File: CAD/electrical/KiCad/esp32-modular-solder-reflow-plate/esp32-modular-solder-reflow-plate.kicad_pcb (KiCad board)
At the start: 2 copper layers, 81.3 x 50.8 mm, 86 parts, among them J1 Thermo Coupler JST, J2 HEATER P, J3 HEATER N, J4 Micro_SD, J5 USB-C, J6 I2C, J7 PWR_IN, J8 Serial, Q1 Heater N-FET, Q2 Q_PMOS_DGS, SW1 µC_BTN01, SW2 µC_BTN02, SW3 µC_BTN03, SW4 µC_BTN04, SW5 µC_EN, SW6 µC_IO0, U1 MAX31855KASA, U2 ESP32-S3-WROOM-2, U3 AMS1117-3.3, U4 AMS1117-5.0, Y1 32k Hz

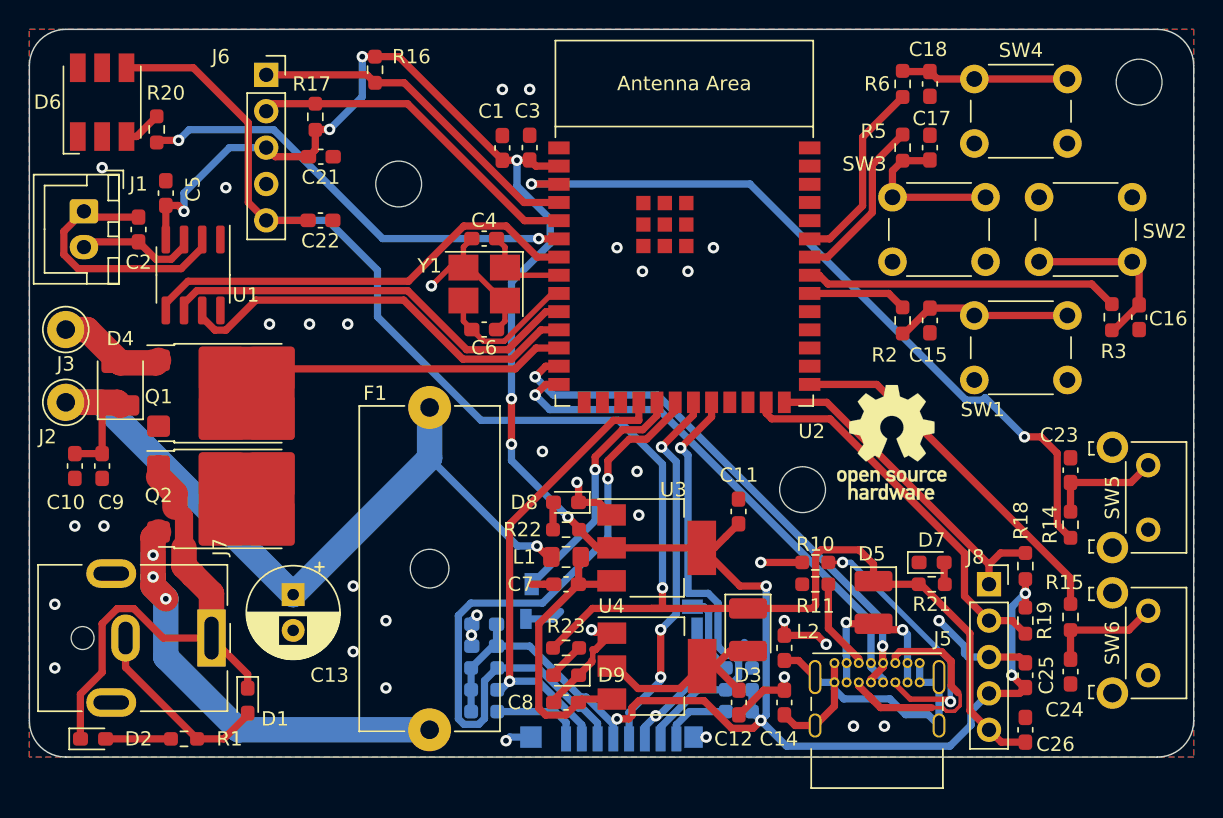
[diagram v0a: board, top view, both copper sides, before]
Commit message: - CAD: pcb routing improvements
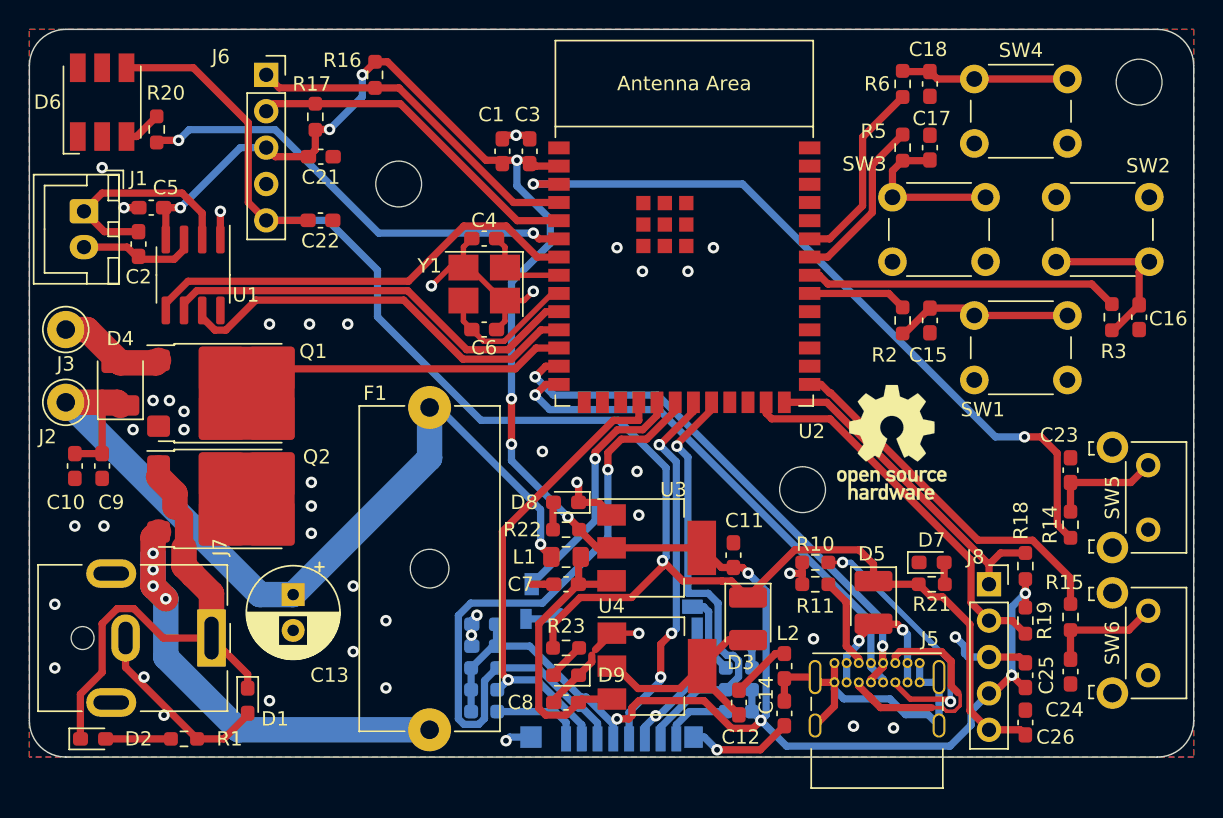
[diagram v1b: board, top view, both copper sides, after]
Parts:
- moved C11 3.07 mm to (172.3, 93.2)
- moved C5 1.44 mm to (131.7, 69.0), turned to 180 degrees
- moved L2 1.27 mm to (175.9, 101.0)
- moved SW2 1.19 mm to (201.4, 72.7)
- moved C2 1.02 mm to (130.8, 71.5)
- moved C14 0.76 mm to (175.9, 104.3), turned to 90 degrees
- moved D3 0.76 mm to (173.4, 97.7)
- moved C26 0.51 mm to (192.7, 104.9)
- moved R16 0.36 mm to (147.3, 59.7)
- moved C3 0.25 mm to (158.1, 65.0)
- moved C1 0.23 mm to (156.2, 65.0)
- turned C12 to 90 degrees
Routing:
- net 3V3_µC: track 162.8 -> 156.7 mm
- net PWR_IN_N: track 80.0 -> 85.0 mm, vias 37 -> 47
- net THCPL_n: track 18.8 -> 15.6 mm
- net HEATER_P: track 59.2 -> 62.1 mm
- net Net-(D3-A): track 13.6 -> 16.0 mm
- net +5V: track 115.1 -> 112.7 mm
- net Net-(D5-A): track 12.2 -> 10.9 mm
- net Net-(J5-SHIELD): track 26.6 -> 25.4 mm
- net Net-(Q2-S): track 33.2 -> 33.3 mm, vias 3 -> 4

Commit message: - CAD: library clean up, routing improvements, new heat bed terminal
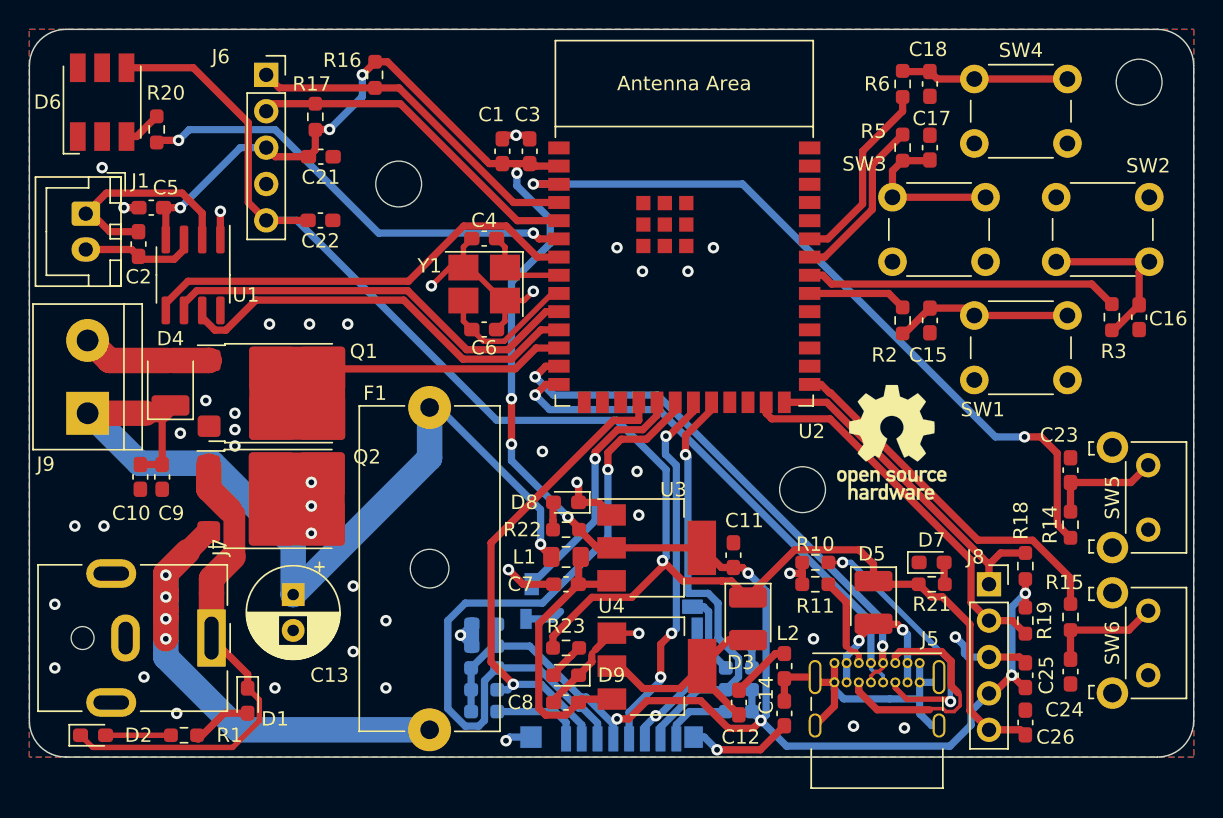
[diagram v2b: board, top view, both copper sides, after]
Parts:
- removed J2: HEATER P, Connector_Pin:Pin_D1.3mm_L11.0mm
- removed J3: HEATER N, Connector_Pin:Pin_D1.3mm_L11.0mm
- added J9: Heater, TerminalBlock:TerminalBlock_bornier-2_P5.08mm, F.Cu at (127.3, 83.3)
- Mount 1: renamed from REF**
- Mount 2: renamed from REF**
- Mount 3: renamed from REF**
- moved C10 4.64 mm to (130.9, 87.8)
- moved C9 4.26 mm to (132.5, 87.8)
- moved Q1 3.53 mm to (140.7, 81.9)
- moved D4 3.50 mm to (133.0, 81.3)
- moved Q2 3.50 mm to (140.7, 89.3)
- moved D2 0.25 mm to (127.6, 105.8)
- moved R1 0.25 mm to (134.0, 105.8)
- moved J1 0.21 mm to (127.1, 69.4)
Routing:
- net PWR_IN_N: track 85.0 -> 79.7 mm
- net HEATER_CTRL: track 20.7 -> 17.1 mm
- net HEATER_P: track 62.1 -> 64.6 mm
- net Net-(Q2-S): track 33.3 -> 35.0 mm
- net +5V: track 112.7 -> 111.0 mm
- net Net-(J5-SHIELD): track 25.4 -> 23.7 mm
- net PWR_IN_P: track 35.7 -> 34.2 mm
- net HEATER_N: track 7.52 -> 8.61 mm
- net SD_CMD: track 48.1 -> 49.1 mm
- net SD_CD: track 33.0 -> 33.8 mm
- net Net-(D9-A): track 2.65 -> 3.40 mm
- net SD_DAT0: track 30.8 -> 30.0 mm
- net USBC_SBU12: track 17.4 -> 16.7 mm
- net THCPL_p: track 8.91 -> 8.27 mm
- net Net-(D8-A): track 1.92 -> 2.55 mm
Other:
- board text added: "Modular Solder Reflow Plate Main Control Board Rev. 0.0.1"

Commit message: - cad: added USB d+ and d- pull up and pull down options; optimized overall component layout; improved silkscreens
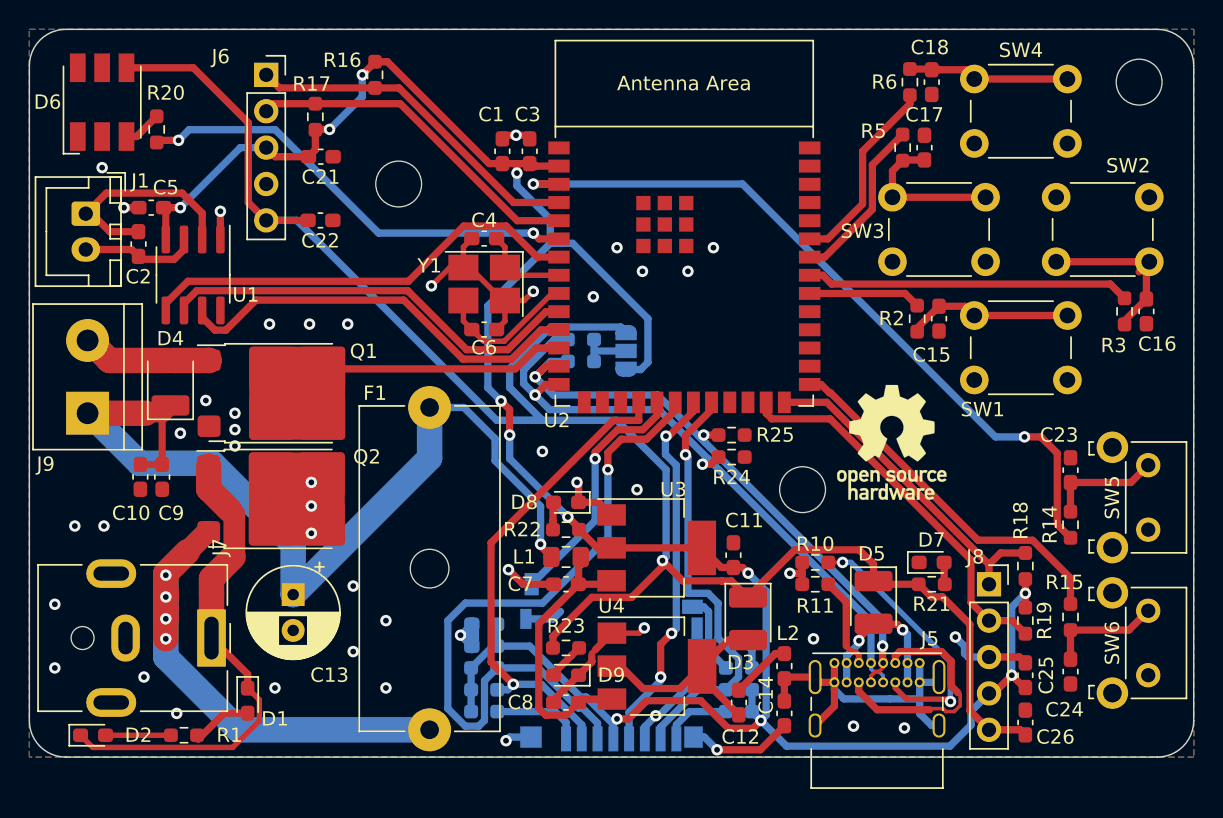
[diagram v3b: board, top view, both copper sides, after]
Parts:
- added JP1: USB_PU, Jumper:SolderJumper-3_P1.3mm_Open_RoundedPad1.0x1.5mm, B.Cu at (164.8, 79.0)
- added R24: 5k1, Resistor_SMD:R_0603_1608Metric_Pad0.98x0.95mm_HandSolder, F.Cu at (172.2, 86.4)
- added R25: 5k1, Resistor_SMD:R_0603_1608Metric_Pad0.98x0.95mm_HandSolder, F.Cu at (172.2, 84.8)
- added R26: 5k1, Resistor_SMD:R_0603_1608Metric_Pad0.98x0.95mm_HandSolder, B.Cu at (161.7, 78.2)
- added R27: 5k1, Resistor_SMD:R_0603_1608Metric_Pad0.98x0.95mm_HandSolder, B.Cu at (161.7, 79.7)
- J1: value Thermo Coupler JST -> Thermo Coupler
- moved R2 1.02 mm to (185.2, 76.7)
- moved R3 0.98 mm to (199.6, 76.2)
- moved C16 0.65 mm to (201.2, 76.2)
- moved C15 0.65 mm to (186.7, 76.7)
- moved R6 0.52 mm to (184.7, 60.2)
- moved C17 0.38 mm to (185.7, 64.8)
- moved C18 0.18 mm to (186.2, 60.2)
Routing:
- net +5V: track 111.0 -> 127.1 mm
- net 3V3_µC: track 156.9 -> 172.1 mm
- net USB_Dp: track 36.8 -> 44.7 mm, vias 1 -> 2
- net USB_Dn: track 38.1 -> 41.9 mm, vias 2 -> 3
- net Net-(JP1-C): track 0.00 -> 3.73 mm
- net HEATER_P: track 64.6 -> 66.3 mm
- net BTN01: track 6.89 -> 7.86 mm
- net Net-(C16-Pad2): track 12.4 -> 13.2 mm
- net BTN02: track 21.9 -> 22.6 mm
- net PWR_IN_N: track 79.7 -> 80.3 mm
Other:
- board text added: "3V3"
- board text added: "5V"

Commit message: - cad: improved routing; added VIN voltage monitoring capability
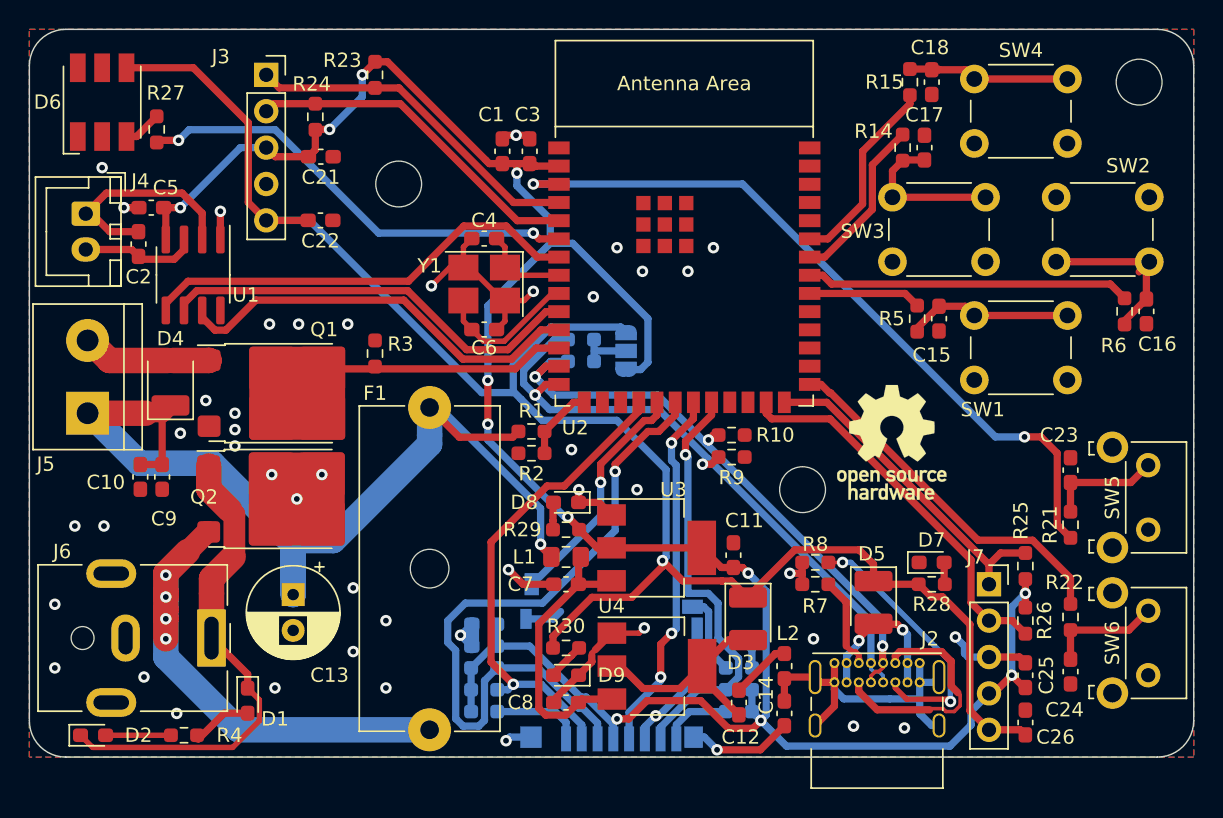
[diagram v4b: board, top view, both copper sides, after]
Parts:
- added R1: 100M, Resistor_SMD:R_0603_1608Metric_Pad0.98x0.95mm_HandSolder, F.Cu at (158.2, 84.6)
- added R2: 15M, Resistor_SMD:R_0603_1608Metric_Pad0.98x0.95mm_HandSolder, F.Cu at (158.2, 86.1)
- added R3: 330, Resistor_SMD:R_0603_1608Metric_Pad0.98x0.95mm_HandSolder, F.Cu at (147.3, 79.1)
- renumbered J4 to J1, J5 to J2, J6 to J3, J1 to J4, J9 to J5, J7 to J6, J8 to J7, R25 to R10, R26 to R11, R27 to R12, R4 to R13, R5 to R14, R6 to R15, R7 to R16, R8 to R17, R9 to R18, R12 to R19, R13 to R20, R14 to R21, R15 to R22, R16 to R23, R17 to R24, R18 to R25, R19 to R26, R20 to R27, R21 to R28, R22 to R29, R23 to R30, R1 to R4, R2 to R5, R3 to R6, R11 to R7, R10 to R8, R24 to R9
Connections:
- U2 pad 15: unconnected-(U2-GPIO3/TOUCH3/ADC1_CH2-Pad15) -> VIN_ADC
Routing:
- net HEATER_P: track 66.3 -> 73.4 mm
- net VIN_ADC: track 0.00 -> 5.14 mm
- net +5V: track 127.1 -> 122.1 mm
- net SD_DET: track 17.4 -> 16.6 mm
- net PWR_IN_N: track 80.3 -> 79.7 mm
- net SD_CMD: track 49.1 -> 48.6 mm

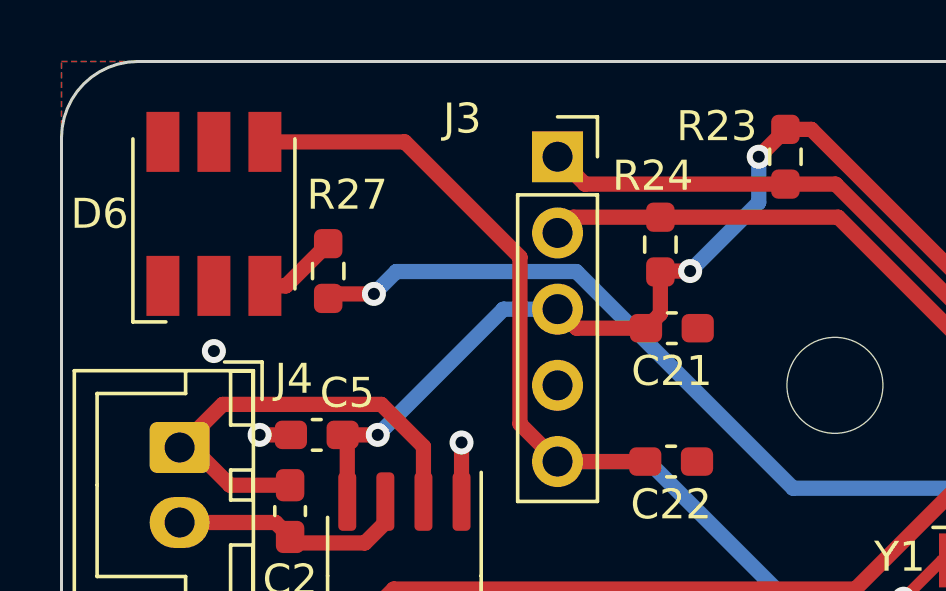
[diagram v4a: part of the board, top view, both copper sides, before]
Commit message: - cad: swapped WS2812 against SK6812Mini
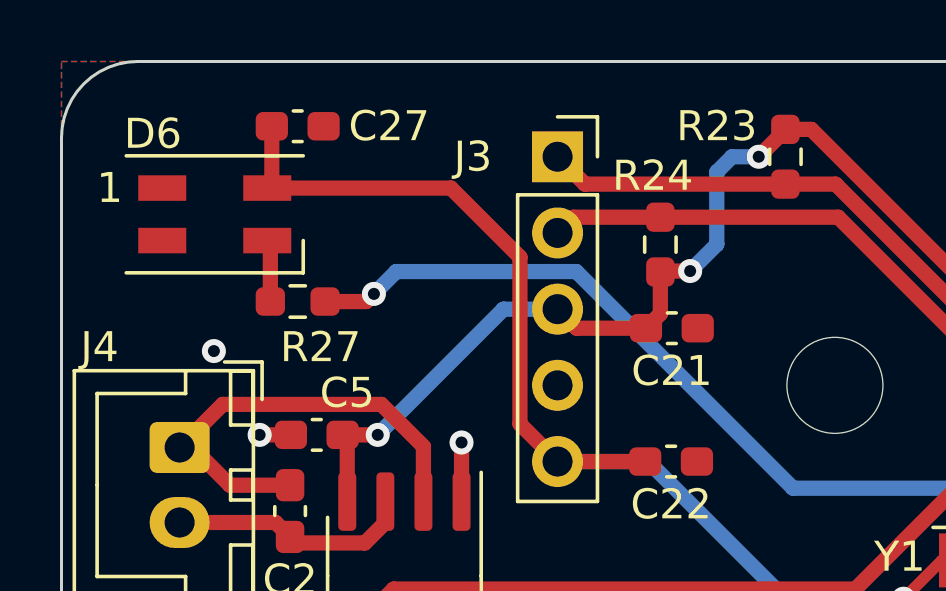
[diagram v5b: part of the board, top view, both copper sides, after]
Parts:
- added C27: 4µ7, Capacitor_SMD:C_0603_1608Metric_Pad1.08x0.95mm_HandSolder, F.Cu at (131.1, 58.7)
- D6: value SK6805 -> SK6812MINI; footprint LED_SMD:LED_RGB_5050-6 -> LED_SMD:LED_SK6812MINI_PLCC4_3.5x3.5mm_P1.75mm
- moved R27 1.44 mm to (131.1, 64.5), turned to 180 degrees
- turned D6 to 0 degrees
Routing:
- net +5V: track 122.1 -> 123.5 mm
- net Net-(D6-DIN): track 2.69 -> 2.07 mm
- net 3V3_µC: track 172.2 -> 172.7 mm

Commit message: - cad: added a buzzer control output
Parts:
- added J8: Buzzer, Connector_JST:JST_XH_B2B-XH-A_1x02_P2.50mm_Vertical, F.Cu at (201.4, 80.5)
- added Q3: BUZ_CTL, Package_TO_SOT_SMD:SOT-23, F.Cu at (188.2, 89.2)
- added R3: 330, Resistor_SMD:R_0603_1608Metric_Pad0.98x0.95mm_HandSolder, F.Cu at (150.4, 80.0)
- added R32: 100, Resistor_SMD:R_0603_1608Metric_Pad0.98x0.95mm_HandSolder, F.Cu at (190.0, 86.6)
- added R33: 1k, Resistor_SMD:R_0603_1608Metric_Pad0.98x0.95mm_HandSolder, F.Cu at (190.0, 85.1)
- added R34: 1k, Resistor_SMD:R_0603_1608Metric_Pad0.98x0.95mm_HandSolder, F.Cu at (191.0, 89.7)
- moved REF** 2.27 mm to (182.4, 83.3)
- moved C23 1.74 mm to (195.8, 89.0)
- moved R22 1.74 mm to (195.8, 92.8)
- moved SW5 1.74 mm to (201.3, 88.7)
- moved SW6 1.49 mm to (201.3, 98.6)
- moved C16 1.44 mm to (202.2, 75.2), turned to 180 degrees
- moved R7 0.72 mm to (199.1, 76.7), turned to 0 degrees
- renumbered R9 to R10, R10 to R11, R11 to R12, R12 to R13, R13 to R14, R14 to R15, R15 to R16, R16 to R17, R17 to R18, R18 to R19, R19 to R20, R20 to R21, R21 to R22, R22 to R23, R23 to R24, R24 to R25, R25 to R26, R26 to R27, R27 to R28, R28 to R29, R29 to R30, R30 to R31, R3 to R4, R4 to R5, R5 to R6, R6 to R7, R7 to R8, R8 to R9
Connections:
- Q1 pad 2: HEATER_CTRL -> Net-(Q1-G)
- R4 pad 1: HEATER_CTRL -> Net-(Q1-G)
- U2 pad 31: unconnected-(U2-GPIO38/FSPIWP/SUBSPIWP-Pad31) -> BUZZER_EN
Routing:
- net +5V: track 123.5 -> 148.2 mm, vias 1 -> 3
- net BUZZER_EN: track 0.00 -> 17.1 mm
- net Net-(J8-Pin_2): track 0.00 -> 15.9 mm, vias 0 -> 1
- net HEATER_CTRL: track 17.1 -> 9.57 mm
- net Net-(Q1-G): track 0.00 -> 5.90 mm
- net Net-(Q3-G): track 0.00 -> 3.73 mm
- net EN: track 52.4 -> 54.4 mm
- net IO0: track 25.6 -> 26.9 mm
- net RX0: track 23.2 -> 24.4 mm
- net TX0: track 27.0 -> 27.9 mm
- net PWR_IN_N: vias 47 -> 51
